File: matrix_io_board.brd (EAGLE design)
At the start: 155.7 x 37.8 mm, 114 parts, among them IC1 6N138, IC2 SN74LVC2G14, IC3 LM27675M5_CHARGEPUMP, IC4 LM324D, IC5 MCP4728_QUAD_DAC, IC6 4504D, IC7 SP34063A_BOOST_REG, IC8 FDS8958B

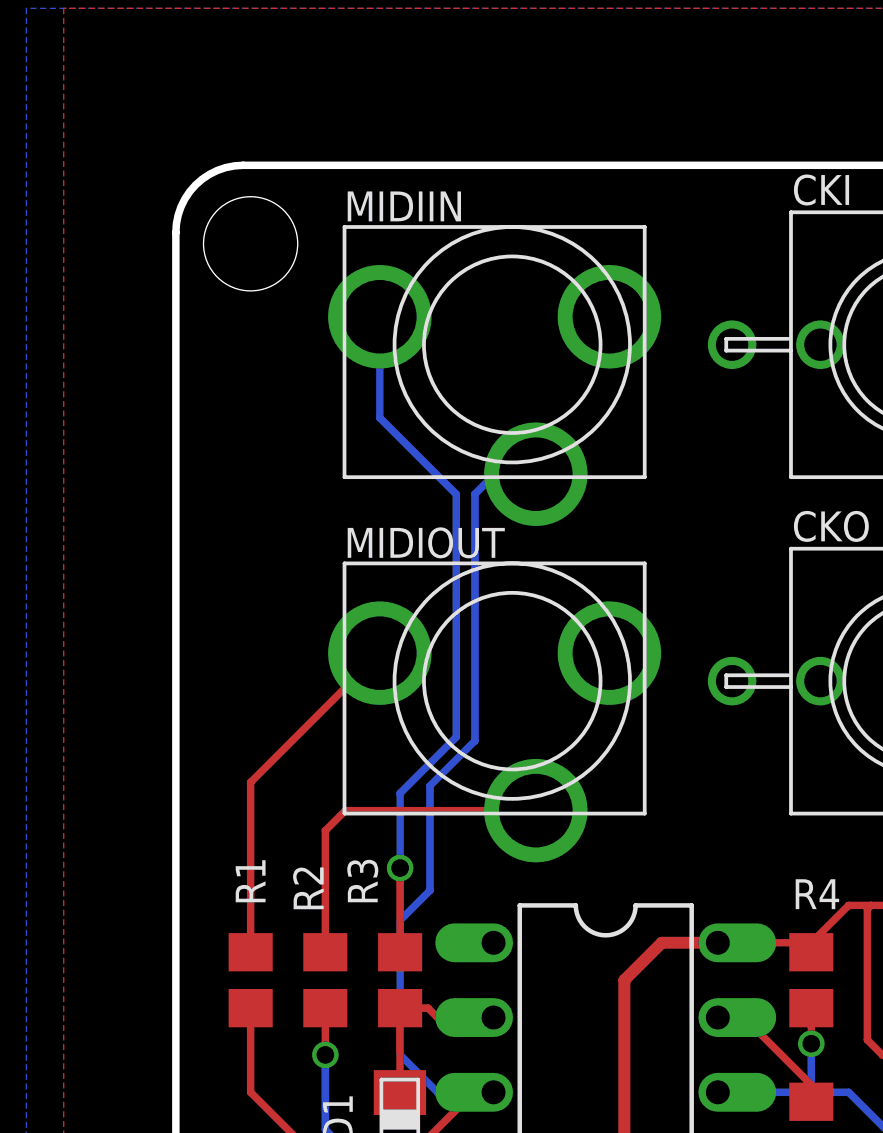
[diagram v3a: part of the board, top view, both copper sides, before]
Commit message: use the new stereo Thonk sockets
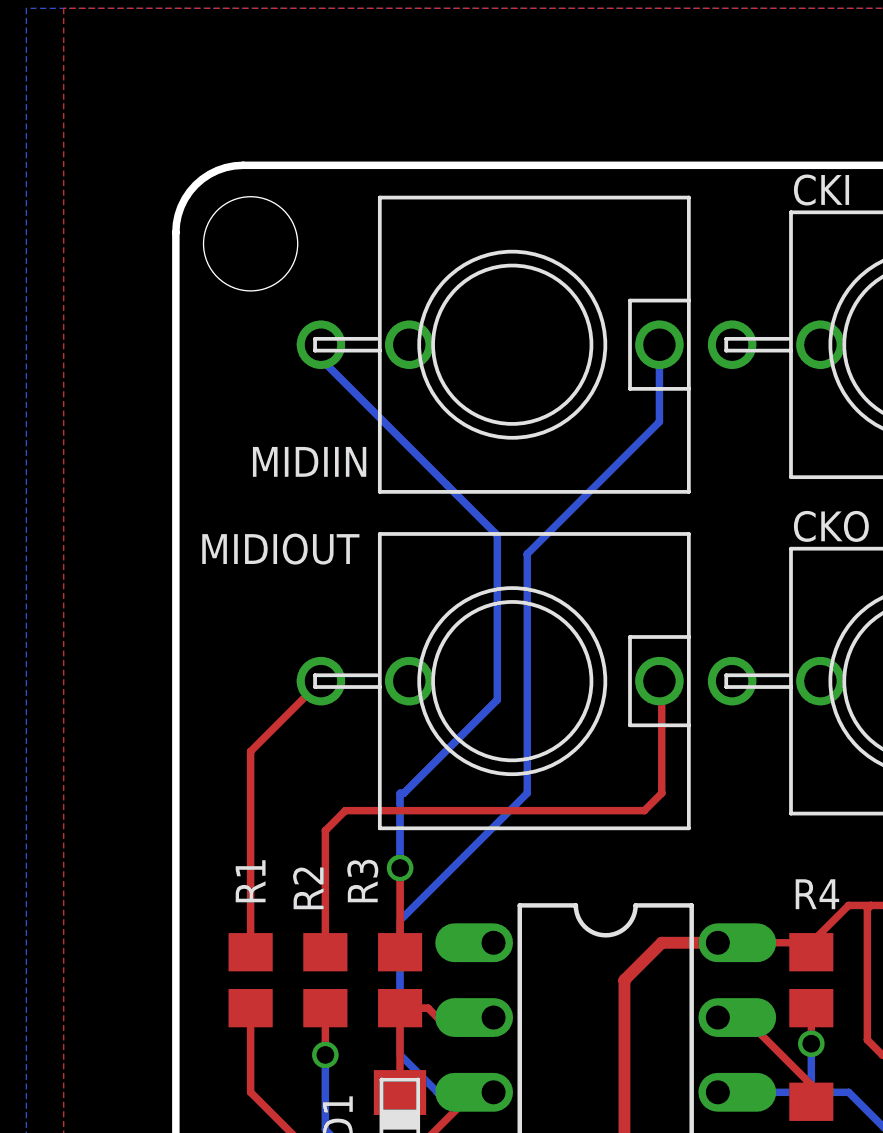
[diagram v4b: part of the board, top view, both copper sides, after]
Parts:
- MIDIIN, MIDIOUT: value VERTICAL_3_5MM_SOCKETASSS -> THONKICONN_STEREO; device jason_eagle6:OFFSET-PINS -> jason_eagle6:WQP-PJ301M-ST
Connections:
- net GND: now also MIDIOUT.P$2; no longer MIDIOUT.P$1
- net N$1: now also MIDIOUT.P$3; no longer MIDIOUT.P$2
- net N$4: now also MIDIIN.P$1; no longer MIDIIN.P$3
- net N$6: now also MIDIOUT.P$1; no longer MIDIOUT.P$3
- net N$7: now also MIDIIN.P$3; no longer MIDIIN.P$2
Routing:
- net N$6: track 11.6 -> 19.9 mm
- net N$4: track 30.4 -> 35.7 mm
- net N$1: track 12.0 -> 10.2 mm
- net N$7: track 23.5 -> 24.6 mm
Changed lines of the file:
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@@
 <attribute name="NAME" x="73.533" y="12.7" size="1.016" layer="25" font="vector" ratio="20" rot="R90"/>
-</element>
-<element name="MIDIOUT" library="jason_eagle6" package="OFFSET-PINS" value="VERTICAL_3_5MM_SOCKETASSS" x="12.7" y="21.59" smashed="yes" rot="R270">
-<attribute name="NAME" x="6.985" y="25.781" size="1.016" layer="21" font="vector" ratio="20"/>
-</element>
-<element name="MIDIIN" library="jason_eagle6" package="OFFSET-PINS" value="VERTICAL_3_5MM_SOCKETASSS" x="12.7" y="33.02" smashed="yes" rot="R270">
-<attribute name="NAME" x="6.985" y="37.211" size="1.016" layer="21" font="vector" ratio="20"/>
 </element>
 <element name="CKO" library="thonkiconn" package="WQP-PJ301M-12_JACK" value="WQP-PJ301M-12_JACK" x="26.67" y="21.59" smashed="yes" rot="R270">
@@
 <element name="GD4" library="pinhead" package="1X01" value="" x="120.65" y="15.24" smashed="yes">
 <attribute name="VALUE" x="119.38" y="12.065" size="1.27" layer="27"/>
+</element>
+<element name="MIDIOUT" library="jason_eagle6" package="WQP-PJ301M-ST" value="THONKICONN_STEREO" x="12.7" y="21.59" smashed="yes" rot="R270">
+<attribute name="NAME" x="2.0446" y="25.5698" size="1.016" layer="21" font="vector" ratio="20"/>
+</element>
+<element name="MIDIIN" library="jason_eagle6" package="WQP-PJ301M-ST" value="THONKICONN_STEREO" x="12.7" y="33.02" smashed="yes" rot="R270">
+<attribute name="NAME" x="7.8614" y="29.5482" size="1.016" layer="21" font="vector" ratio="20" rot="R180"/>
 </element>
 </elements>
@@
 <contactref element="IC1" pad="3"/>
 <contactref element="D1" pad="C"/>
-<contactref element="MIDIIN" pad="P$3"/>
 <wire x1="12.065" y1="7.62" x2="11.3932" y2="7.62" width="0.254" layer="1"/>
 <wire x1="11.3932" y1="7.62" x2="8.885" y2="5.1118" width="0.254" layer="1"/>
-<wire x1="13.5" y1="28.62" x2="12.11" y2="28.62" width="0.254" layer="16"/>
-<wire x1="12.11" y1="28.62" x2="11.43" y2="27.94" width="0.254" layer="16"/>
-<wire x1="11.43" y1="27.94" x2="11.43" y2="19.558" width="0.254" layer="16"/>
-<wire x1="11.43" y1="19.558" x2="9.906" y2="18.034" width="0.254" layer="16"/>
-<wire x1="9.906" y1="18.034" x2="9.906" y2="14.478" width="0.254" layer="16"/>
-<wire x1="9.906" y1="14.478" x2="8.89" y2="13.462" width="0.254" layer="16"/>
 <wire x1="8.89" y1="13.462" x2="8.89" y2="8.89" width="0.254" layer="16"/>
 <wire x1="8.89" y1="8.89" x2="10.16" y2="7.62" width="0.254" layer="16"/>
 <wire x1="10.16" y1="7.62" x2="12.065" y2="7.62" width="0.254" layer="16"/>
+<contactref element="MIDIIN" pad="P$1"/>
+<wire x1="17.7" y1="33.02" x2="17.7" y2="30.4" width="0.254" layer="16"/>
+<wire x1="8.89" y1="13.462" x2="13.208" y2="17.78" width="0.254" layer="16"/>
+<wire x1="13.208" y1="17.78" x2="13.208" y2="25.908" width="0.254" layer="16"/>
+<wire x1="13.208" y1="25.908" x2="17.7" y2="30.4" width="0.254" layer="16"/>
 </signal>
 <signal name="N$5">
@@
 <contactref element="D5" pad="C"/>
 <contactref element="C1" pad="2"/>
-<contactref element="MIDIOUT" pad="P$1"/>
 <contactref element="GD3" pad="1"/>
 <contactref element="GD4" pad="1"/>
@@
 <via x="137.033" y="36.449" extent="1-16" drill="0.6"/>
 <via x="131.064" y="30.734" extent="1-16" drill="0.6"/>
+<contactref element="MIDIOUT" pad="P$2"/>
 </signal>
 <signal name="+5V">
@@
 <signal name="N$6">
 <contactref element="R2" pad="1"/>
-<contactref element="MIDIOUT" pad="P$3"/>
-<wire x1="13.5" y1="17.19" x2="7.03" y2="17.19" width="0.254" layer="1"/>
 <wire x1="7.03" y1="17.19" x2="6.35" y2="16.51" width="0.254" layer="1"/>
 <wire x1="6.35" y1="16.51" x2="6.35" y2="12.38" width="0.254" layer="1"/>
+<contactref element="MIDIOUT" pad="P$1"/>
+<wire x1="7.03" y1="17.19" x2="17.19" y2="17.19" width="0.254" layer="1"/>
+<wire x1="17.19" y1="17.19" x2="17.78" y2="17.78" width="0.254" layer="1"/>
+<wire x1="17.78" y1="17.78" x2="17.78" y2="21.51" width="0.254" layer="1"/>
+<wire x1="17.78" y1="21.51" x2="17.7" y2="21.59" width="0.254" layer="1"/>
 </signal>
 <signal name="MIDI_OUT">
@@
 <contactref element="DC" pad="BARREL"/>
 <wire x1="143.51" y1="28.82" x2="150.758" y2="28.82" width="0.4064" layer="1"/>
-<wire x1="150.758" y1="28.82" x2="152.654" y2="26.924" width="0.4064" layer="1"/>
 <wire x1="152.654" y1="26.924" x2="152.654" y2="25.7125" width="0.4064" layer="1"/>
 <wire x1="152.654" y1="25.7125" x2="152.776" y2="25.5905" width="0.4064" layer="1"/>
+<wire x1="150.758" y1="28.82" x2="152.654" y2="26.924" width="0.4064" layer="1"/>
 </signal>
 <signal name="N$10">
@@
 <wire x1="140.97" y1="12.7" x2="142.24" y2="13.97" width="0.254" layer="1"/>
 <wire x1="142.24" y1="13.97" x2="142.24" y2="17.78" width="0.254" layer="1"/>
-<wire x1="142.24" y1="17.78" x2="140.208" y2="19.812" width="0.254" layer="1"/>
 <wire x1="140.208" y1="19.812" x2="136.398" y2="19.812" width="0.254" layer="1"/>
 <wire x1="136.398" y1="19.812" x2="135.89" y2="20.32" width="0.254" layer="1"/>
@@
 <wire x1="135.89" y1="23.622" x2="136.398" y2="24.13" width="0.254" layer="1"/>
 <wire x1="136.398" y1="24.13" x2="139.192" y2="24.13" width="0.254" layer="1"/>
-<wire x1="139.192" y1="24.13" x2="140.081" y2="25.019" width="0.254" layer="1"/>
-<wire x1="140.081" y1="25.019" x2="140.081" y2="29.083" width="0.254" layer="1"/>
 <wire x1="140.081" y1="29.083" x2="135.636" y2="33.528" width="0.254" layer="1"/>
 <wire x1="135.636" y1="33.528" x2="135.57" y2="33.528" width="0.254" layer="1"/>
 <wire x1="135.57" y1="33.528" x2="135.189" y2="33.909" width="0.254" layer="1"/>
+<wire x1="139.192" y1="24.13" x2="140.081" y2="25.019" width="0.254" layer="1"/>
+<wire x1="142.24" y1="17.78" x2="140.208" y2="19.812" width="0.254" layer="1"/>
+<wire x1="140.081" y1="25.019" x2="140.081" y2="29.083" width="0.254" layer="1"/>
 </signal>
 <signal name="VIN">
@@
 <signal name="N$7">
 <contactref element="R3" pad="1"/>
-<contactref element="MIDIIN" pad="P$2"/>
 <wire x1="8.89" y1="12.38" x2="8.89" y2="15.24" width="0.254" layer="1"/>
 <via x="8.89" y="15.24" extent="1-16" drill="0.6"/>
-<wire x1="8.2" y1="33.97" x2="8.2" y2="30.535" width="0.254" layer="16"/>
-<wire x1="8.2" y1="30.535" x2="10.795" y2="27.94" width="0.254" layer="16"/>
-<wire x1="10.795" y1="27.94" x2="10.795" y2="19.685" width="0.254" layer="16"/>
-<wire x1="10.795" y1="19.685" x2="8.89" y2="17.78" width="0.254" layer="16"/>
+<wire x1="6.2" y1="32.535" x2="10.4775" y2="28.2575" width="0.254" layer="16"/>
+<wire x1="10.4775" y1="28.2575" x2="10.795" y2="27.94" width="0.254" layer="16"/>
 <wire x1="8.89" y1="17.78" x2="8.89" y2="15.24" width="0.254" layer="16"/>
+<contactref element="MIDIIN" pad="P$3"/>
+<wire x1="6.2" y1="33.02" x2="6.2" y2="32.535" width="0.254" layer="16"/>
+<wire x1="8.89" y1="17.78" x2="9.017" y2="17.78" width="0.254" layer="16"/>
+<wire x1="9.017" y1="17.78" x2="12.192" y2="20.955" width="0.254" layer="16"/>
+<wire x1="12.192" y1="20.955" x2="12.192" y2="26.543" width="0.254" layer="16"/>
+<wire x1="12.192" y1="26.543" x2="10.795" y2="27.94" width="0.254" layer="16"/>
 </signal>
 <signal name="N$1">
 <contactref element="R1" pad="1"/>
-<contactref element="MIDIOUT" pad="P$2"/>
-<wire x1="3.81" y1="12.38" x2="3.81" y2="18.15" width="0.254" layer="1"/>
-<wire x1="3.81" y1="18.15" x2="8.2" y2="22.54" width="0.254" layer="1"/>
+<wire x1="3.81" y1="12.38" x2="3.81" y2="19.2" width="0.254" layer="1"/>
+<contactref element="MIDIOUT" pad="P$3"/>
+<wire x1="3.81" y1="19.2" x2="6.2" y2="21.59" width="0.254" layer="1"/>
 </signal>
 <signal name="N$16">

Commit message: V4 ready to go
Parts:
- renumbered BATT+ to BT+, BATT- to BT-
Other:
- board text added: "NOODLEBOX I/O BOARD V4"
- board text removed: "NOODLEBOX I/O BOARD V3"
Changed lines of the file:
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@@
 <hole x="3.81" y="36.449" drill="3.2"/>
 <hole x="154.432" y="36.449" drill="3.2"/>
-<text x="6.7945" y="38.5445" size="2.54" layer="52" font="vector" ratio="20" rot="MR180">NOODLEBOX I/O BOARD V3</text>
+<text x="6.7945" y="38.5445" size="2.54" layer="52" font="vector" ratio="20" rot="MR180">NOODLEBOX I/O BOARD V4</text>
 <wire x1="1.27" y1="36.83" x2="3.556" y2="39.116" width="0.254" layer="20" curve="-90"/>
 <wire x1="119.38" y1="15.24" x2="118.745" y2="15.24" width="0.254" layer="21"/>
@@
 <elements>
 <element name="DC" library="jason_eagle6" package="PWR_SOCKET_2_1MM" value="PWR_SOCKET_2_1MM" x="143.51" y="33.02" smashed="yes" rot="R180">
-<attribute name="NAME" x="151.765" y="38.1" size="1.016" layer="21" font="vector" ratio="20" rot="R180"/>
+<attribute name="NAME" x="139.954" y="38.354" size="1.016" layer="21" font="vector" ratio="20" rot="R180"/>
 </element>
 <element name="PWR" library="led" package="LED3MM" value="" x="143.51" y="20.32" smashed="yes" rot="R270">
@@
 <attribute name="VALUE" x="106.595" y="1.5598" size="1.27" layer="27" rot="R90"/>
 </element>
-<element name="BATT+" library="pinhead" package="1X01" value="" x="152.527" y="31.623" smashed="yes">
-<attribute name="NAME" x="151.1808" y="33.4518" size="1.016" layer="25" font="vector" ratio="20"/>
+<element name="BT+" library="pinhead" package="1X01" value="" x="152.527" y="31.623" smashed="yes">
+<attribute name="NAME" x="153.2382" y="30.1752" size="1.016" layer="25" font="vector" ratio="20" rot="R180"/>
 <attribute name="VALUE" x="151.257" y="28.448" size="1.27" layer="27"/>
 </element>
-<element name="BATT-" library="pinhead" package="1X01" value="" x="155.067" y="31.623" smashed="yes">
-<attribute name="NAME" x="153.7208" y="33.4518" size="1.016" layer="25" font="vector" ratio="20"/>
+<element name="BT-" library="pinhead" package="1X01" value="" x="155.067" y="31.623" smashed="yes">
+<attribute name="NAME" x="153.8478" y="29.1338" size="1.016" layer="25" font="vector" ratio="20"/>
 <attribute name="VALUE" x="153.797" y="28.448" size="1.27" layer="27"/>
 </element>
@@
 <contactref element="D2" pad="C"/>
 <contactref element="DC" pad="PIN"/>
-<contactref element="BATT-" pad="1"/>
+<contactref element="BT-" pad="1"/>
 <contactref element="R6" pad="1"/>
 <contactref element="C5" pad="1"/>
@@
 </signal>
 <signal name="N$16">
-<contactref element="BATT+" pad="1"/>
+<contactref element="BT+" pad="1"/>
 <contactref element="DC" pad="NC"/>
 <wire x1="152.527" y1="31.623" x2="149.107" y2="31.623" width="0.4064" layer="1"/>

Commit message: V5 first cut
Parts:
- C10, C11, C12, C5, C6, C7: value 100n -> 10n
- C19, C20, C22: device rcl:E2,5-7 -> rcl:PANASONIC_D
- D7: value CGRM4001-G -> MBR0520LT; device diode:SOD-123_MINI-SMA -> diode:SOD123
- moved C20 1.30 mm to (79.8, 5.59), turned to 0 degrees
- moved C19 1.27 mm to (79.8, 12.8), turned to 0 degrees
- moved C22 0.09 mm to (151.1, 11.4), turned to 0 degrees
- moved D7 0.06 mm to (90.6, 6.73)
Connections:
- net GND: now also MIDIOUT.P$3; no longer MIDIOUT.P$2
- net N$1: now also MIDIOUT.P$2; no longer MIDIOUT.P$3
- net N$7: now also MIDIIN.P$2; no longer MIDIIN.P$3
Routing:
- net +9V: track 141.0 -> 143.9 mm, vias 3 -> 4
- net N$51: track 42.6 -> 39.8 mm
- net N$7: track 24.6 -> 23.3 mm
- net N$1: track 10.2 -> 11.4 mm
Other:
- board text added: "+"
- board text added: "JP1"
- board text added: "NOODLEBOX I/O BOARD V5"
- board text removed: "NOODLEBOX I/O BOARD V4"
